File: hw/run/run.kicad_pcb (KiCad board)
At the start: 2 copper layers, 38.4 x 58.9 mm, 21 parts, among them J1 conn_trigger, J2 conn_done, J3 FTDI, J4 conn_active, SW1 switch_active, SW2 switch_active, SW3 switch_reset, U1 ATmega328P-PU, Y1 Crystal

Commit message: RUN block v2
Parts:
- removed J2: conn_done, Connector_PinHeader_2.54mm:PinHeader_1x03_P2.54mm_Vertical
- removed J4: conn_active, Connector_PinHeader_2.54mm:PinHeader_1x03_P2.54mm_Vertical
- added D2: DIODE, Diode_SMD:D_0603_1608Metric, F.Cu at (134.1, 122.7)
- added H5: led_spy_hole, MountingHole:MountingHole_3.2mm_M3, F.Cu at (151.6, 105.9)
- added J5: BUS, Connector_PinHeader_2.54mm:PinHeader_2x07_P2.54mm_Vertical, F.Cu at (149.1, 95.0)
- added R4: 10k, Resistor_SMD:R_0603_1608Metric, F.Cu at (146.2, 113.4)
- added R7: 1k, Resistor_SMD:R_0603_1608Metric, F.Cu at (146.5, 123.5)
- added SW4: NEXT, Package_DIP:DIP-16_W7.62mm_SMDSocket_SmallPads, F.Cu at (136.4, 141.7)
- added SW5: ACTIVE, Package_DIP:DIP-16_W7.62mm_SMDSocket_SmallPads, F.Cu at (136.4, 130.3)
- added SW6: ID, Package_DIP:DIP-16_W7.62mm_SMDSocket_SmallPads, F.Cu at (136.4, 153.2)
- C1: footprint Capacitor_THT:CP_Radial_Tantal_D6.0mm_P2.50mm -> Capacitor_SMD:C_0603_1608Metric
- C2, C3: footprint Capacitor_THT:C_Disc_D3.0mm_W1.6mm_P2.50mm -> Capacitor_SMD:C_0603_1608Metric
- C4, C5: footprint Capacitor_THT:C_Axial_L5.1mm_D3.1mm_P7.50mm_Horizontal -> Capacitor_SMD:C_0603_1608Metric
- D1: moved to B.Cu
- H1, H2, H3, H4: footprint MountingHole:MountingHole_2.2mm_M2 -> MountingHole:MountingHole_3.2mm_M3_Pad
- J1: value conn_trigger -> bootloader; footprint Connector_PinHeader_2.54mm:PinHeader_1x03_P2.54mm_Vertical -> autoblocks:edge_connector_3
- J3: footprint Connector_PinHeader_2.54mm:PinHeader_1x06_P2.54mm_Vertical -> autoblocks:edge_connector_3
- R1, R2: footprint Resistor_THT:R_Axial_DIN0207_L6.3mm_D2.5mm_P10.16mm_Horizontal -> Resistor_SMD:R_0603_1608Metric
- SW1: value switch_active -> runSwitch; moved to B.Cu
- SW2: value switch_active -> active; footprint autoblocks:SW_PUSH_6mm_H5mm -> Button_Switch_SMD:SW_SPST_TL3305C
- SW3: value switch_reset -> reset; footprint autoblocks:SW_PUSH_6mm_H5mm -> Button_Switch_SMD:SW_SPST_TL3305C
- U1: value ATmega328P-PU -> ATmega328-AU; footprint Package_DIP:DIP-28_W7.62mm -> Package_QFP:TQFP-32_7x7mm_P0.8mm
- Y1: footprint Crystal:Crystal_HC18-U_Vertical -> Crystal:Crystal_SMD_HC49-SD
- moved SW1 60.8 mm to (144.5, 160.6), turned to 180 degrees
- moved H2 55.2 mm to (128.0, 166.6)
- moved H1 53.5 mm to (154.7, 166.6)
- moved C3 45.3 mm to (146.5, 121.4)
- moved C2 40.9 mm to (146.3, 119.4), turned to 0 degrees
- moved Y1 37.0 mm to (152.4, 117.8), turned to 270 degrees
- moved R1 35.2 mm to (141.0, 106.9), turned to 0 degrees
- moved D1 34.9 mm to (150.1, 103.2), turned to 0 degrees
- moved SW2 33.2 mm to (145.8, 104.4), turned to 90 degrees
- moved C5 30.5 mm to (136.9, 103.1), turned to 0 degrees
- moved H3 29.5 mm to (154.7, 96.8)
- moved H4 29.1 mm to (128.0, 96.8)
- moved C1 26.6 mm to (146.3, 117.5), turned to 180 degrees
- moved C4 25.8 mm to (136.9, 106.9), turned to 180 degrees
- moved R2 24.7 mm to (133.1, 106.8), turned to 180 degrees
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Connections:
- C1 pad 1: VCC -> bus11
- C1 pad 2: GND -> bus13
- C2 pad 1: GND -> bus13
- C3 pad 1: GND -> bus13
- C4 pad 2: GND -> bus13
- D1 pad 1: GND -> bus13
- H1 pad 1: GND -> Net-(H1-Pad1)
- H2 pad 1: GND -> Net-(H2-Pad1)
- H3 pad 1: GND -> Net-(H3-Pad1)
- H4 pad 1: GND -> Net-(H4-Pad1)
- J1 pad 1: a0 -> bus13
- J1 pad 2: GND -> bus11
- J1 pad 3: VCC -> d10
- J3 pad 1: GND -> bus13
- J3 pad 2: GND -> bus13
- J3 pad 3: VCC -> bus11
- R2 pad 1: VCC -> bus11
- SW1 pad 2: GND -> bus13
- SW1 pad 3: Net-(SW1-Pad3) -> (no net)
- SW1 pad 4: Net-(SW1-Pad4) -> (no net)
- SW2 pad 2: GND -> bus13
- SW3 pad 1: GND -> bus13
- U1 pad 1: RESET -> d3
- U1 pad 10: XTAL2 -> d6
- U1 pad 11: d5 -> d7
- U1 pad 12: d6 -> d8
- U1 pad 13: d7 -> d9
- U1 pad 14: d8 -> d10
- U1 pad 15: d9 -> d11
- U1 pad 16: d10 -> d12
- U1 pad 17: d11 -> d13
- U1 pad 18: d12 -> bus11
- U1 pad 19: d13 -> Net-(U1-Pad19)
- U1 pad 2: RX -> d4
- U1 pad 20: VCC -> AREF
- U1 pad 21: AREF -> bus13
- U1 pad 22: GND -> Net-(U1-Pad22)
- U1 pad 3: TX -> bus13
- U1 pad 4: d2 -> bus11
- U1 pad 5: d3 -> bus13
- U1 pad 6: d4 -> bus11
- U1 pad 7: VCC -> XTAL1
- U1 pad 8: GND -> XTAL2
- U1 pad 9: XTAL1 -> d5
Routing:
- net GND: track 233.7 -> 0.00 mm
- net VCC: track 142.5 -> 0.00 mm
- net d10: track 0.00 -> 128.6 mm, vias 0 -> 2
- net d12: track 0.00 -> 126.1 mm, vias 0 -> 3
- net bus11: track 0.00 -> 125.6 mm, vias 0 -> 7
- net d11: track 0.00 -> 114.8 mm, vias 0 -> 1
- net bus13: track 0.00 -> 81.1 mm, vias 0 -> 4
- net bus2: track 0.00 -> 68.0 mm, vias 0 -> 1
- net bus7: track 0.00 -> 62.9 mm, vias 0 -> 1
- net bus3: track 0.00 -> 62.5 mm, vias 0 -> 1
- net bus1: track 0.00 -> 62.1 mm, vias 0 -> 1
- net bus5: track 0.00 -> 59.9 mm, vias 0 -> 1
- net bus8: track 0.00 -> 59.4 mm, vias 0 -> 1
- net bus4: track 0.00 -> 59.0 mm, vias 0 -> 1
- net d13: track 0.00 -> 58.8 mm, vias 0 -> 3
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- added copper zone on B.Cu, net bus11
- added copper zone on F.Cu, net bus13
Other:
- board size 38.4 x 58.9 mm -> 34.3 x 77.5 mm
- rule trace_min: 0.2 -> 0.16
- board text added: "BOOT"
- board text added: "FTDI"
- board text added: "First"
- board text added: "ID"
- board text added: "NEXT"
- board text added: "Next"
- board text added: "active"
- board text added: "v2"
- board text removed: "ACTIVE"
- board text removed: "IN"
- board text removed: "RTS"
- board text removed: "v1"

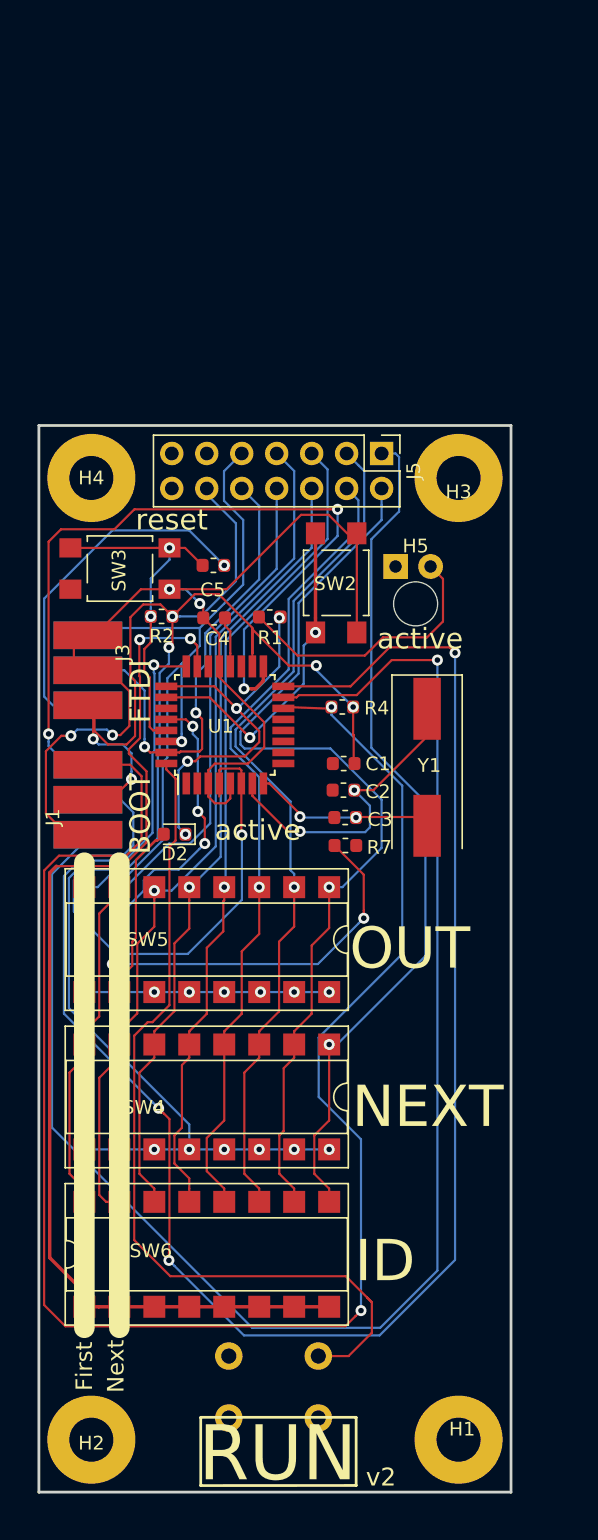
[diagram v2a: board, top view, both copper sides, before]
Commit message: fix RUN bus assigments
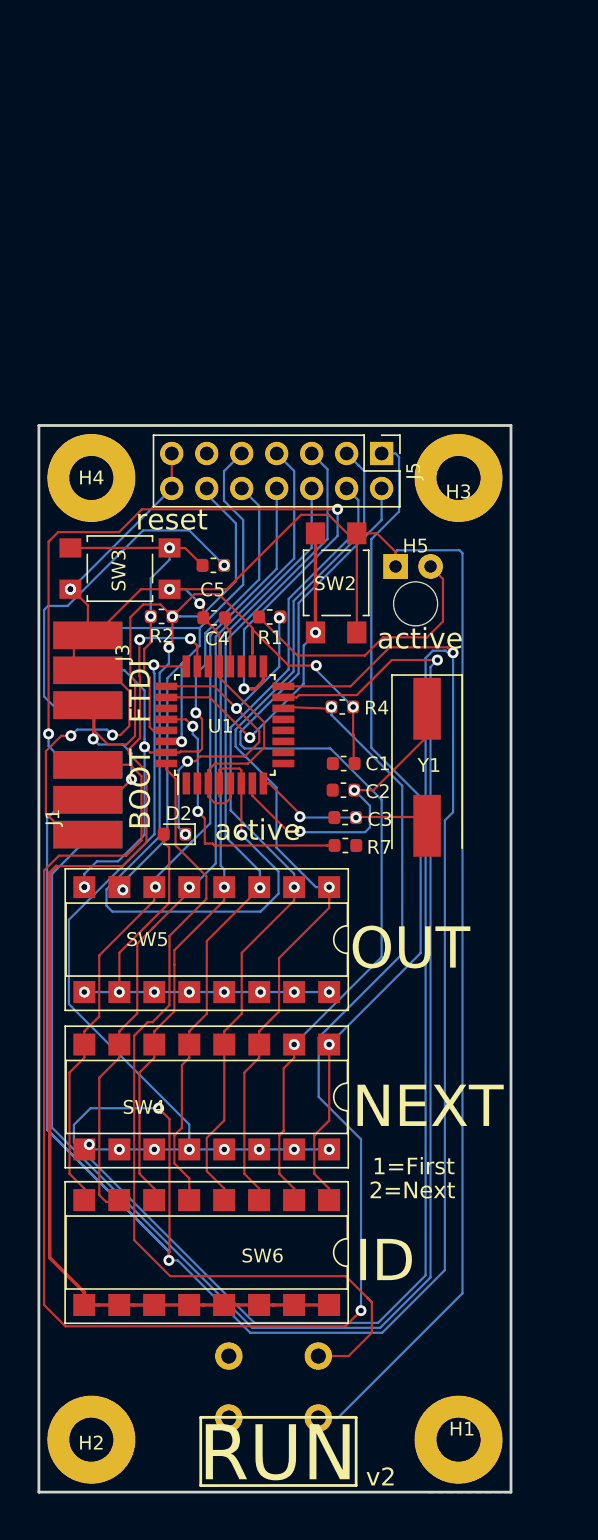
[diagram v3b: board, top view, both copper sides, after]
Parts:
- moved SW6 0.13 mm to (136.4, 153.0), turned to 270 degrees
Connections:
- SW5 pad 1: bus2 -> bus3
- SW5 pad 2: bus3 -> bus4
- SW5 pad 3: bus4 -> bus5
- SW5 pad 4: bus5 -> bus6
- SW5 pad 5: bus6 -> bus7
- SW5 pad 6: bus7 -> bus8
- SW5 pad 7: bus8 -> RX
- SW5 pad 8: RX -> TX
- SW6 pad 1: a0 -> bus1
- SW6 pad 10: bus2 -> a0
- SW6 pad 11: bus3 -> a0
- SW6 pad 12: bus4 -> a0
- SW6 pad 13: bus5 -> a0
- SW6 pad 14: bus6 -> a0
- SW6 pad 15: bus7 -> a0
- SW6 pad 16: bus8 -> a0
- SW6 pad 2: a0 -> bus2
- SW6 pad 3: a0 -> bus3
- SW6 pad 4: a0 -> bus4
- SW6 pad 5: a0 -> bus5
- SW6 pad 6: a0 -> bus6
- SW6 pad 7: a0 -> bus7
- SW6 pad 8: a0 -> bus8
- SW6 pad 9: bus1 -> a0
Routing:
- net d12: track 126.1 -> 234.5 mm
- net bus13: track 81.1 -> 176.4 mm, vias 4 -> 6
- net a5: track 49.4 -> 20.5 mm, vias 6 -> 2
- net TX: track 35.8 -> 48.7 mm, vias 2 -> 4
- net bus11: track 125.6 -> 121.2 mm
- net bus3: track 62.5 -> 66.1 mm
- net bus4: track 59.0 -> 61.1 mm
- net bus5: track 59.9 -> 62.0 mm
- net a1: track 63.3 -> 61.4 mm
- net d2: track 62.7 -> 64.6 mm
- net RX: track 55.3 -> 53.6 mm
- net bus8: track 59.4 -> 58.7 mm
- net Net-(D2-Pad2): track 31.5 -> 30.9 mm
- net bus1: track 62.1 -> 61.4 mm
- net bus7: track 62.9 -> 62.3 mm
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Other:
- board text added: "1=First"
- board text added: "2=Next"
- board text removed: "First"
- board text removed: "Next"
